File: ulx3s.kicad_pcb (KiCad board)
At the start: 4 copper layers, 94 x 50.8 mm, 113 parts, among them J1 CONN_02X20, J2 CONN_02X20, J3 WIFI_OFF, Q1 BC857, Q2 2N7002, U1 LFE5U-25F-6BG381C, U10 S25FL164K0XMFI011, U11 PCA9306DCTR, U2 ESP-32S, U3 AP3429A, U4 AP3429A, U5 AP3429A, U6 FT231XS, U7 PCF8523, U9 MT48LC16M16A2TG, Y1 FNETHE025, Y2 32768Hz

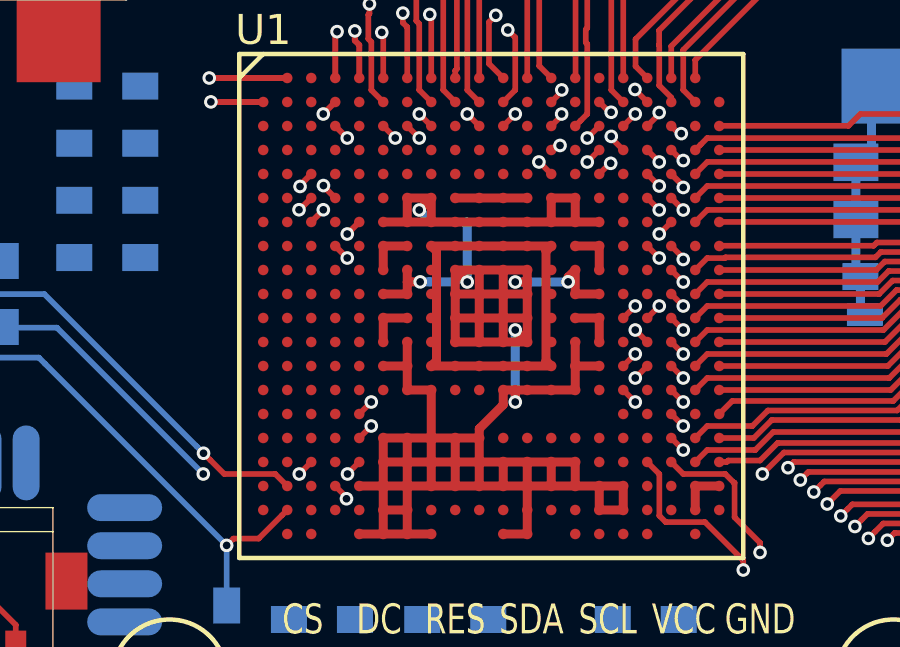
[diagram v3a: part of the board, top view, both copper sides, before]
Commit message: placing copper fill zones for power supply by the book similar to TN1074
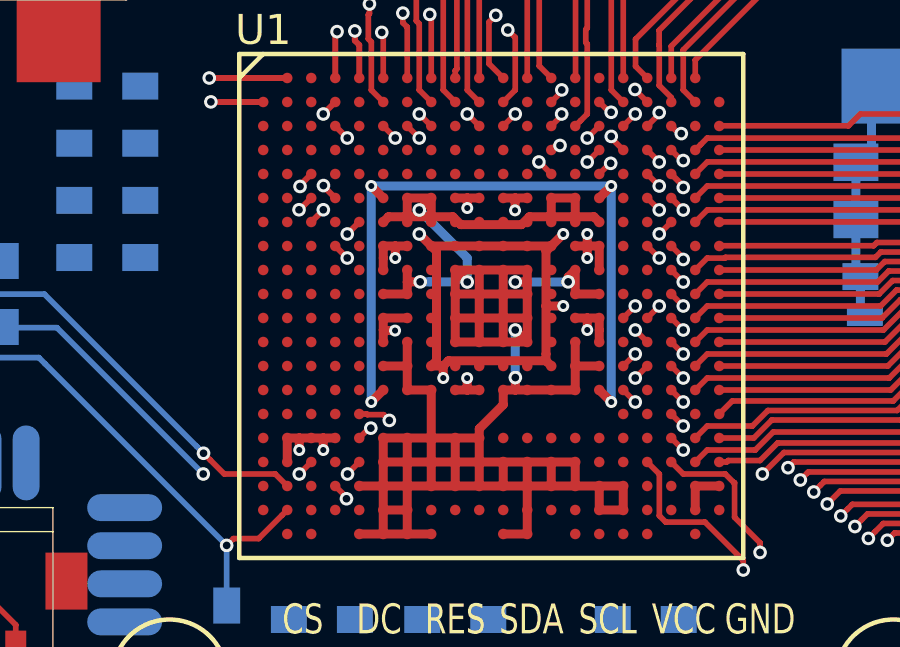
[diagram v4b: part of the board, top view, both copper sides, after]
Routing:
- net +2V5: track 7.96 -> 32.6 mm, vias 0 -> 4
- net +3V3: track 16.8 -> 23.1 mm, vias 0 -> 10
- net +1V2: track 24.1 -> 26.1 mm, vias 0 -> 4
- net GND: track 131.6 -> 130.5 mm
- added copper zone on In1.Cu, net +1V2
- added copper zone on In1.Cu, net +3V3
- added copper zone on In2.Cu, net GND
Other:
- net class Default: via_dia 0.454 -> 0.4; via_drill 0.254 -> 0.2

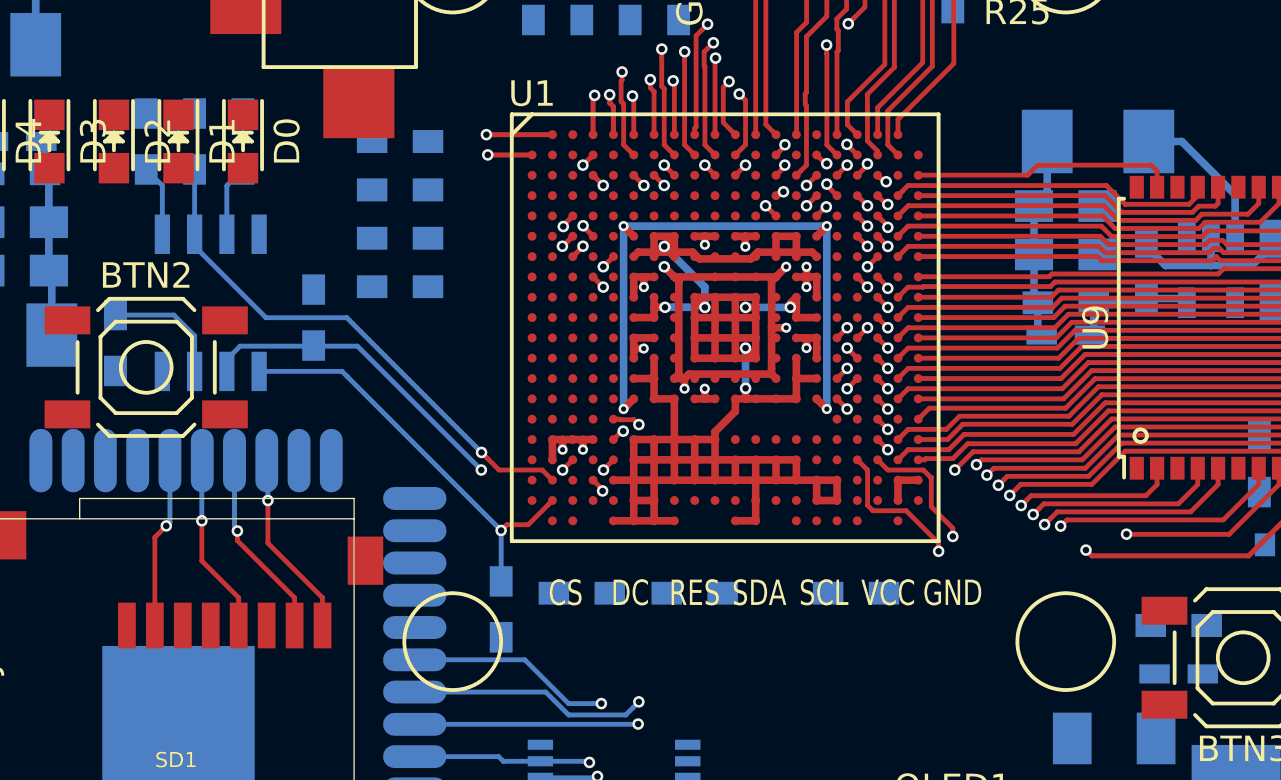
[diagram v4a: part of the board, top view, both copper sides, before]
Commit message: scrapping current routing, placing power supply on copper zones under the BGA
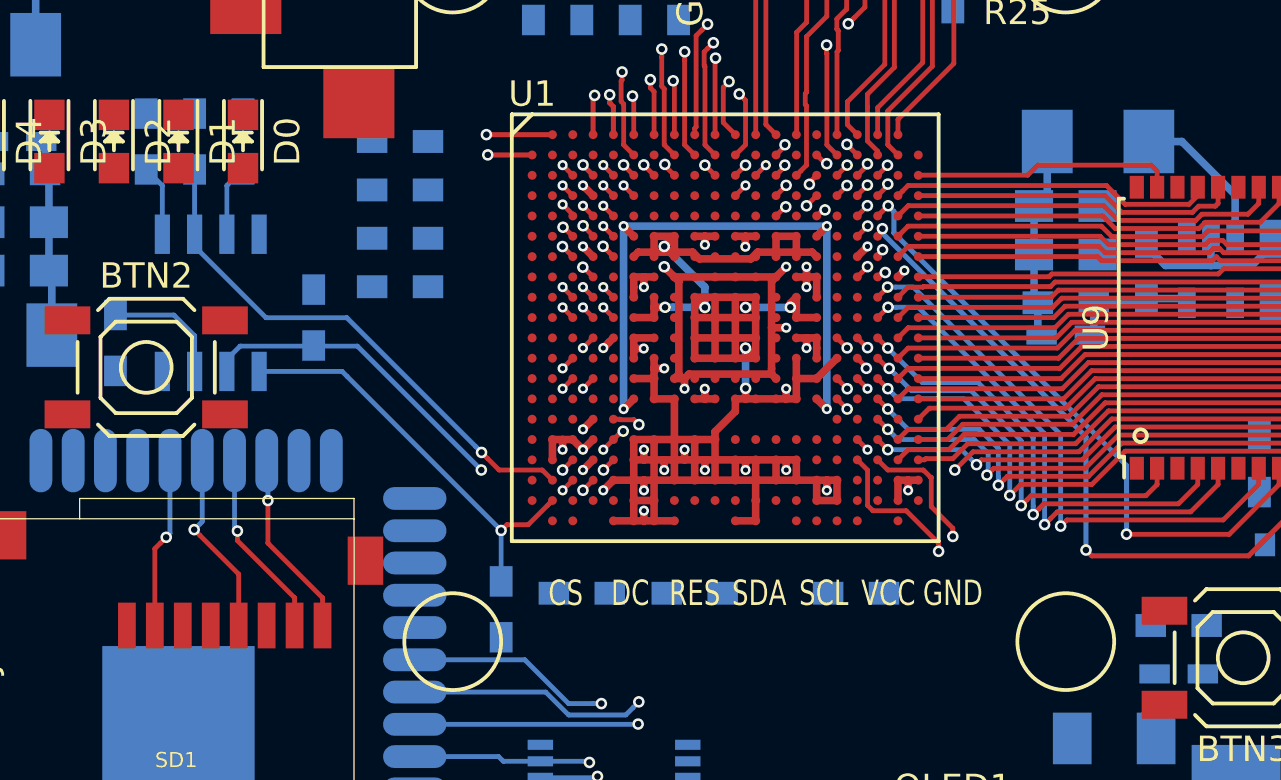
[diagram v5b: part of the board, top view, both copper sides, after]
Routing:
- net J2_23-: track 41.7 -> 0.58 mm
- net J2_17-: track 43.9 -> 11.9 mm
- net J2_15+: track 46.8 -> 16.2 mm
- net J1_33+: track 46.7 -> 18.8 mm
- net J1_35+: track 47.0 -> 19.1 mm
- net J1_33-: track 44.2 -> 16.7 mm
- net J1_35-: track 44.8 -> 17.4 mm
- net J1_31+: track 46.8 -> 19.7 mm
- net J1_29-: track 43.5 -> 17.1 mm, vias 1 -> 0
- net J1_29+: track 46.4 -> 20.3 mm
- net J1_31-: track 42.7 -> 17.2 mm
- net J2_11+: track 50.9 -> 41.0 mm
- net GND: track 130.5 -> 140.2 mm, vias 7 -> 26
- net J2_9-: track 49.0 -> 39.5 mm
- net J2_11-: track 47.9 -> 38.4 mm
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
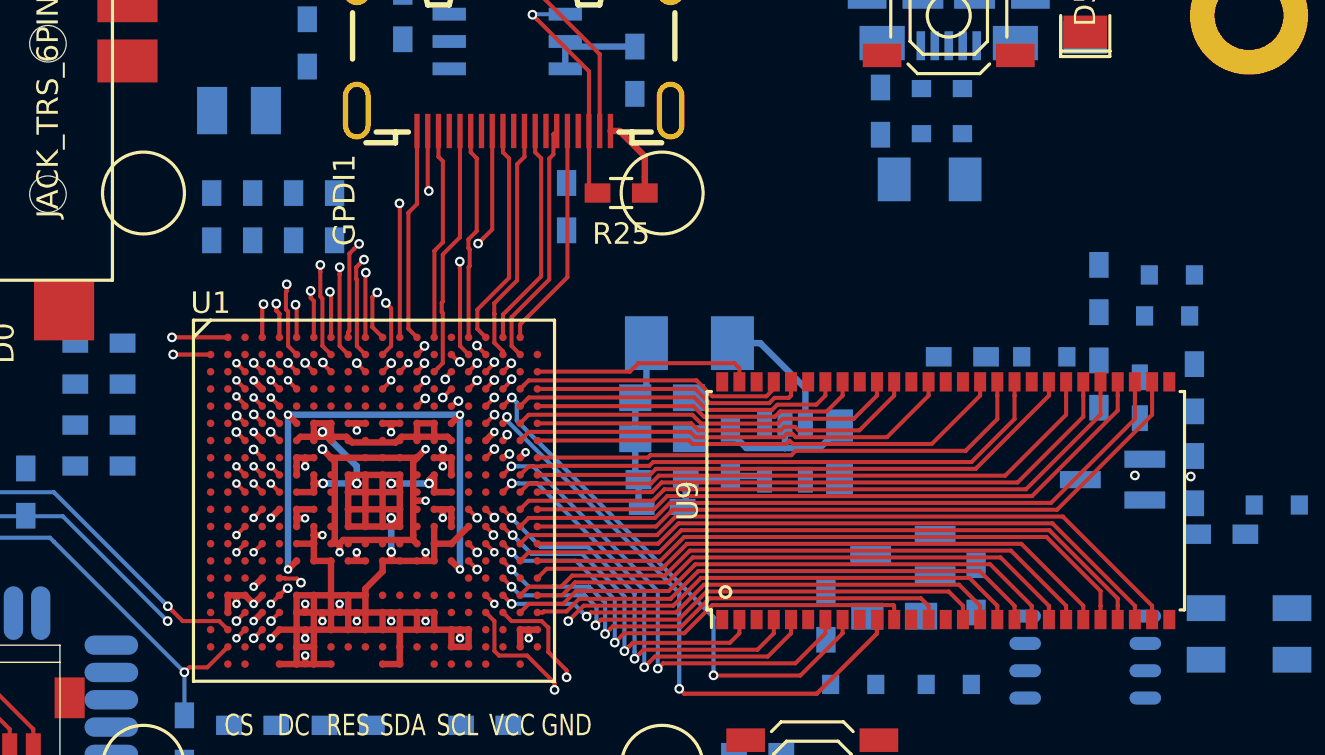
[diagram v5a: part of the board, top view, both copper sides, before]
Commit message: moving routing out of inner layers under BGA to allow larger copper fill zone for power supply
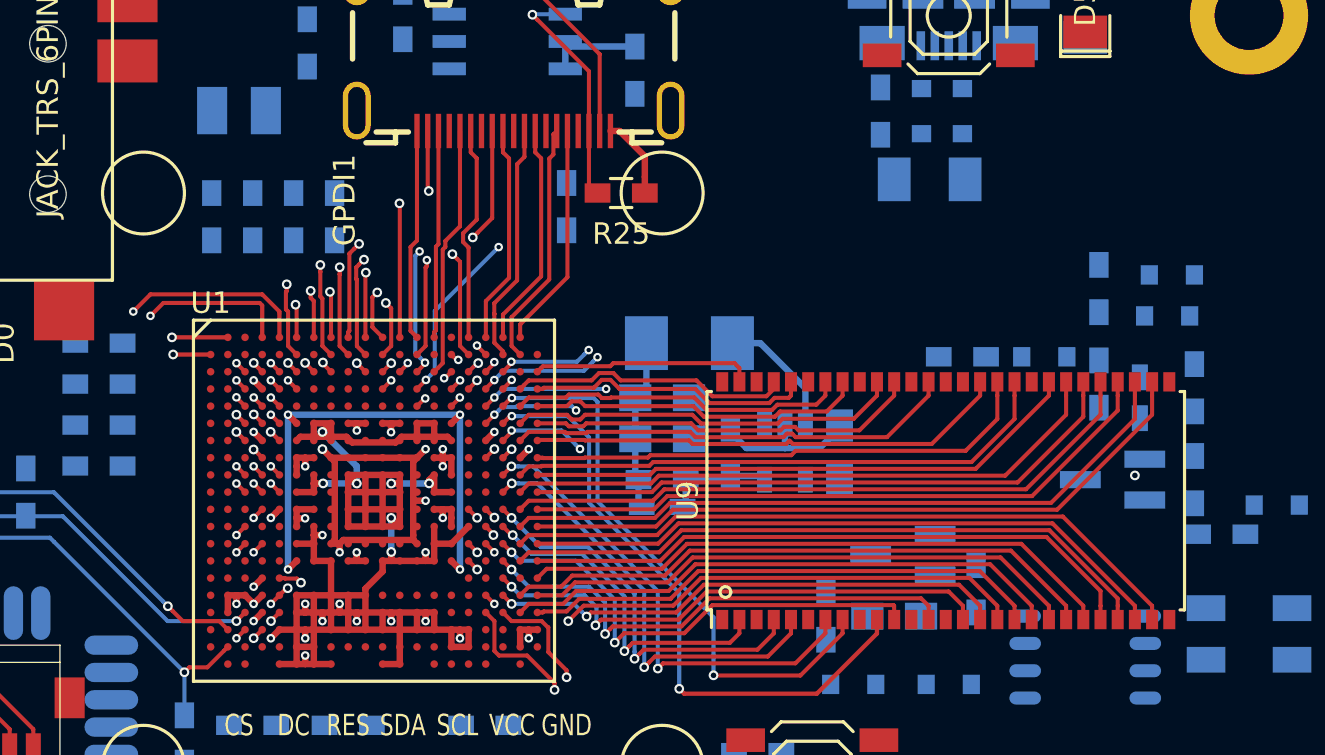
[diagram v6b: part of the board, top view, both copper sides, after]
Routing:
- net J2_23-: track 0.58 -> 42.0 mm, vias 1 -> 2
- net J2_25-: track 38.9 -> 2.64 mm
- net J2_17-: track 11.9 -> 44.3 mm, vias 1 -> 2
- net J2_15+: track 16.2 -> 47.5 mm, vias 1 -> 2
- net J2_33-: track 51.6 -> 37.9 mm
- net J2_29-: track 47.3 -> 37.3 mm
- net J2_35-: track 48.8 -> 53.2 mm, vias 1 -> 2
- net SDRAM_D4: track 24.9 -> 27.1 mm
- net SDRAM_D5: track 27.4 -> 29.1 mm
- net J2_23+: track 43.2 -> 43.9 mm, vias 1 -> 2
- net J2_25+: track 41.2 -> 40.7 mm
- net J2_33+: vias 1 -> 2
- net /flash/FLASH_SCK: vias 2 -> 1

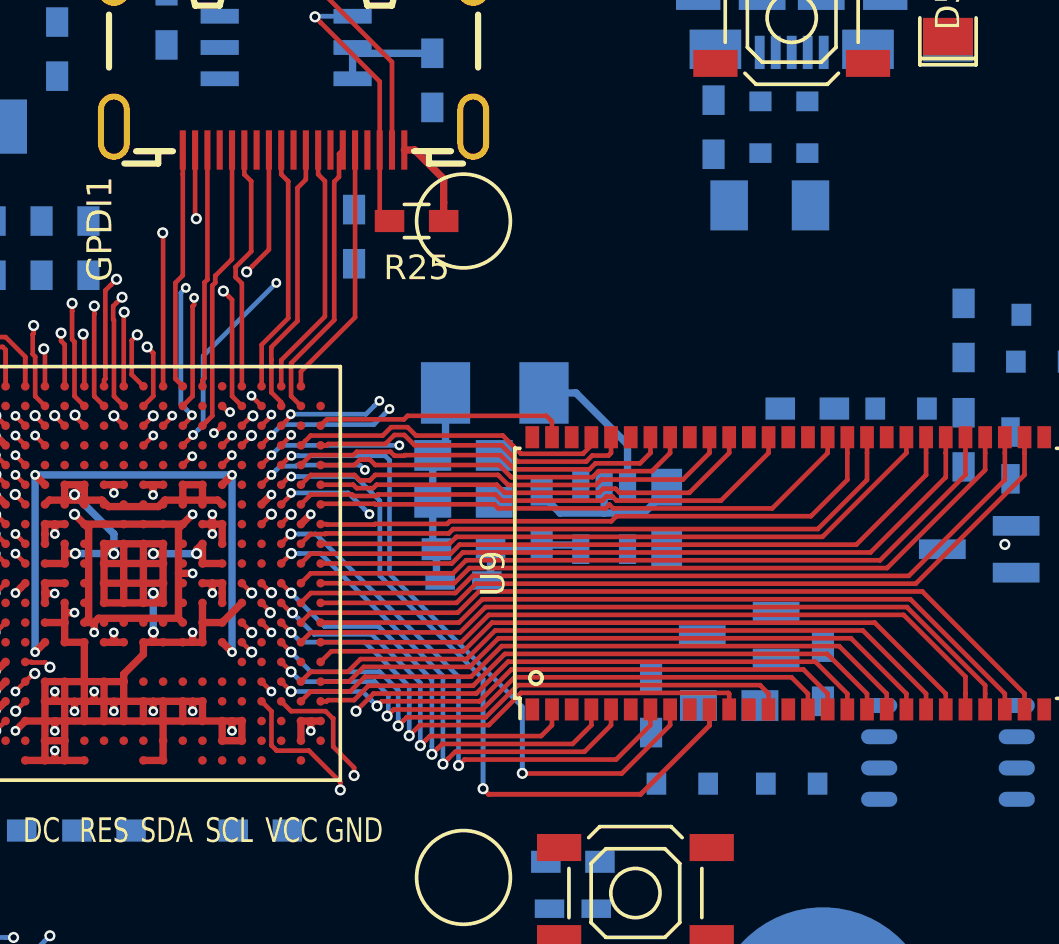
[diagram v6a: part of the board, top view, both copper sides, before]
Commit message: moving routes under BGA out of inner layers
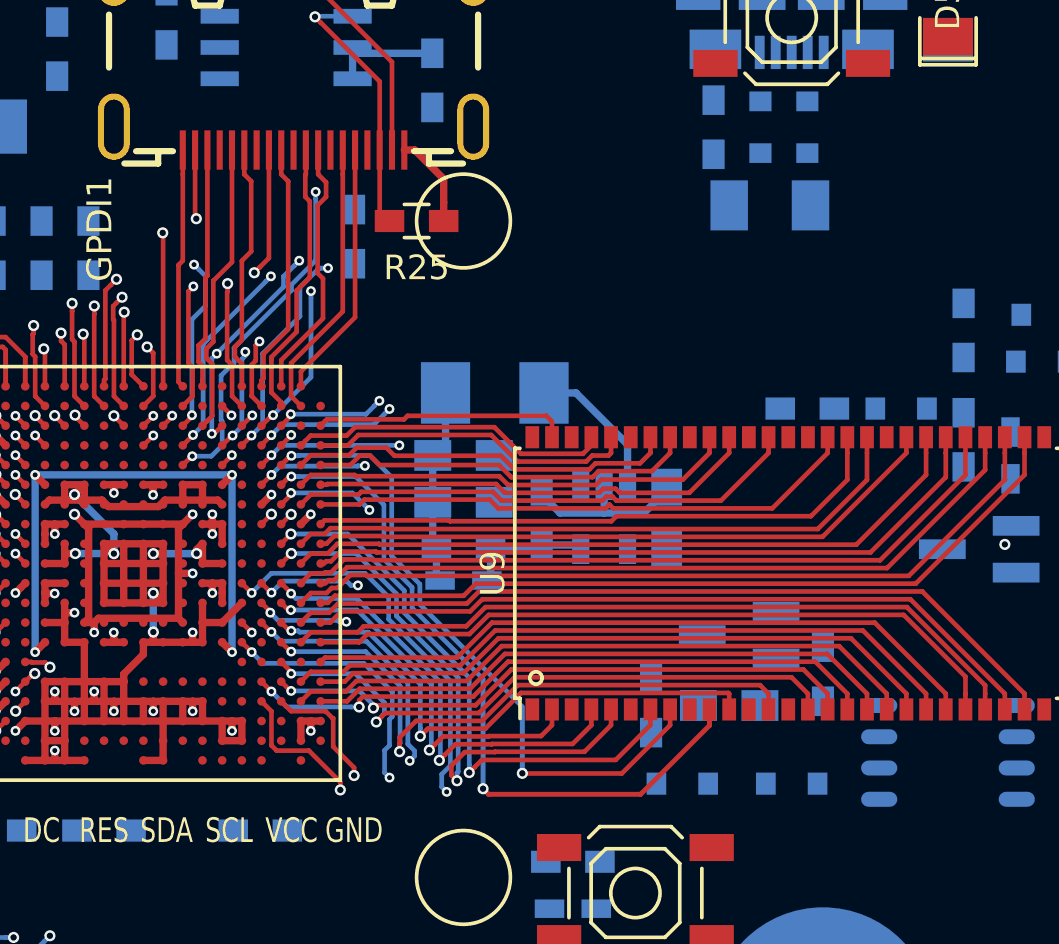
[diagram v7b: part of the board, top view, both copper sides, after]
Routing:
- net J2_33-: track 37.9 -> 53.1 mm, vias 1 -> 2
- net J2_11+: track 41.0 -> 52.3 mm, vias 1 -> 2
- net J2_29-: track 37.3 -> 46.8 mm, vias 1 -> 2
- net J2_25+: track 40.7 -> 49.8 mm, vias 1 -> 2
- net J2_7-: track 40.7 -> 49.1 mm, vias 1 -> 2
- net J2_7+: track 43.3 -> 51.7 mm, vias 1 -> 2
- net J2_9+: track 42.1 -> 49.8 mm
- net J2_11-: track 38.4 -> 45.1 mm, vias 1 -> 2
- net J2_9-: track 39.5 -> 45.5 mm, vias 1 -> 2
- net SDRAM_nCAS: track 22.5 -> 26.3 mm
- net J2_29+: track 48.1 -> 50.3 mm
- net SDRAM_D2: track 20.5 -> 22.7 mm
- net SDRAM_D7: track 23.5 -> 25.5 mm
- net J2_27-: track 44.0 -> 45.6 mm, vias 1 -> 2
- net J2_27+: track 46.1 -> 47.6 mm
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
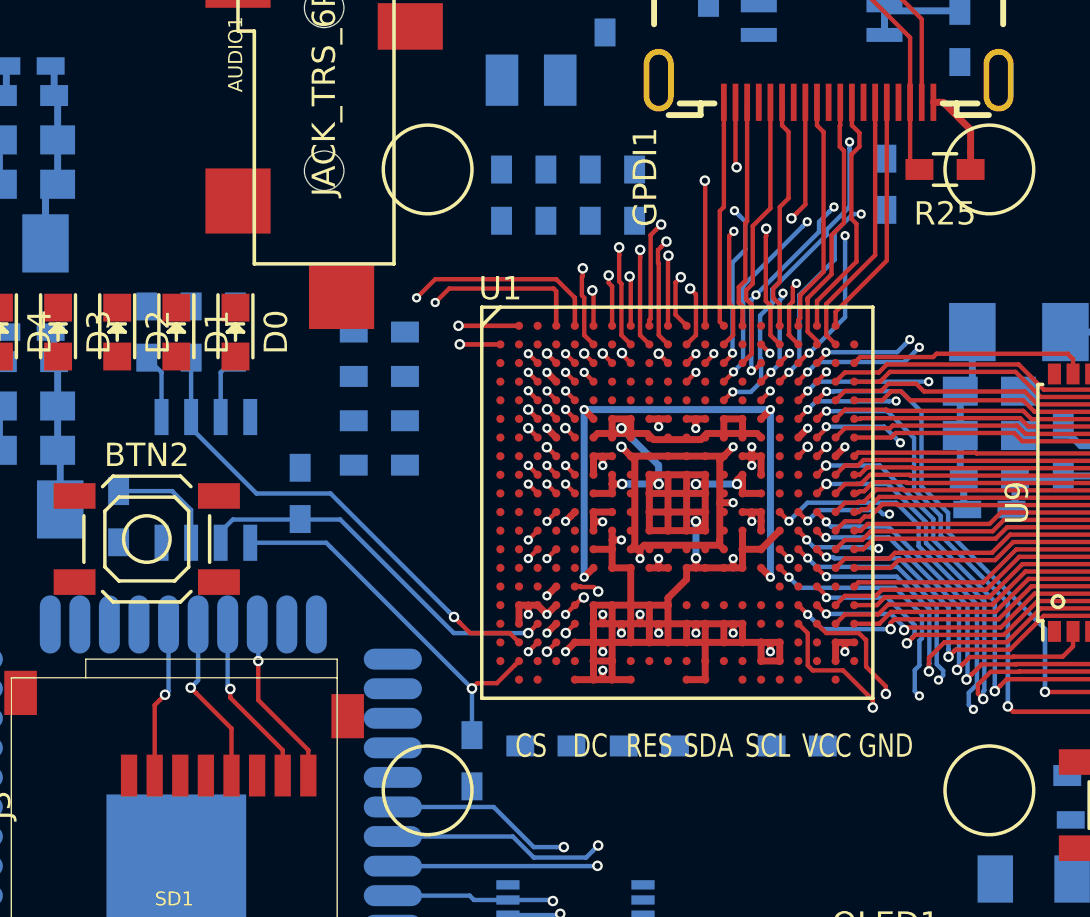
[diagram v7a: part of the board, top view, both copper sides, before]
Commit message: moving inner layer routes away from BGA
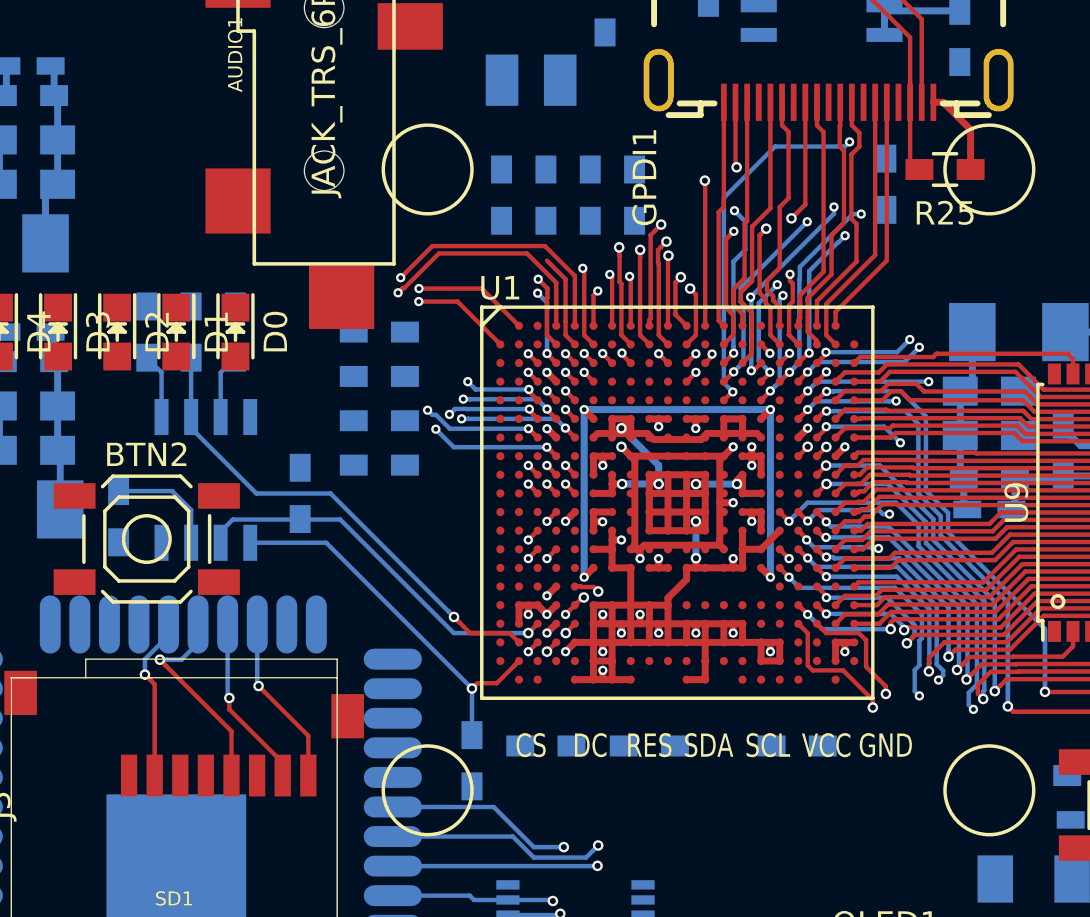
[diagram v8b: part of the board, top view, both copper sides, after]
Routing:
- net J2_25-: track 2.66 -> 47.8 mm, vias 1 -> 2
- net J1_29-: track 17.1 -> 47.0 mm, vias 0 -> 1
- net J1_29+: track 20.3 -> 49.9 mm, vias 1 -> 2
- net J1_35+: track 19.1 -> 47.6 mm, vias 1 -> 2
- net J1_35-: track 17.4 -> 45.6 mm, vias 1 -> 2
- net J1_33+: track 18.8 -> 46.6 mm, vias 1 -> 2
- net J1_31+: track 19.7 -> 46.4 mm, vias 1 -> 2
- net J1_31-: track 17.2 -> 43.4 mm, vias 1 -> 2
- net J1_33-: track 16.8 -> 42.9 mm, vias 1 -> 2
- net AUDIO_L1: track 0.00 -> 4.10 mm
- net J1_17-: track 44.4 -> 46.1 mm
- net SD_CLK: track 7.35 -> 8.99 mm
- net J2_33-: track 53.1 -> 54.6 mm
- net J1_25+: track 46.6 -> 48.0 mm
- net J1_23+: track 47.7 -> 49.0 mm
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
